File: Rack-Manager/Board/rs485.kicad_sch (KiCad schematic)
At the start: 0 parts

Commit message: Updated Texas Instruments and WIZnet KiCAD libraries. Continued with the schematics design.
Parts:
- added U8, U9: THVD1450DRBR, Texas Instruments:DRB0008F, symbol Texas Instruments:THVD1450DRBR

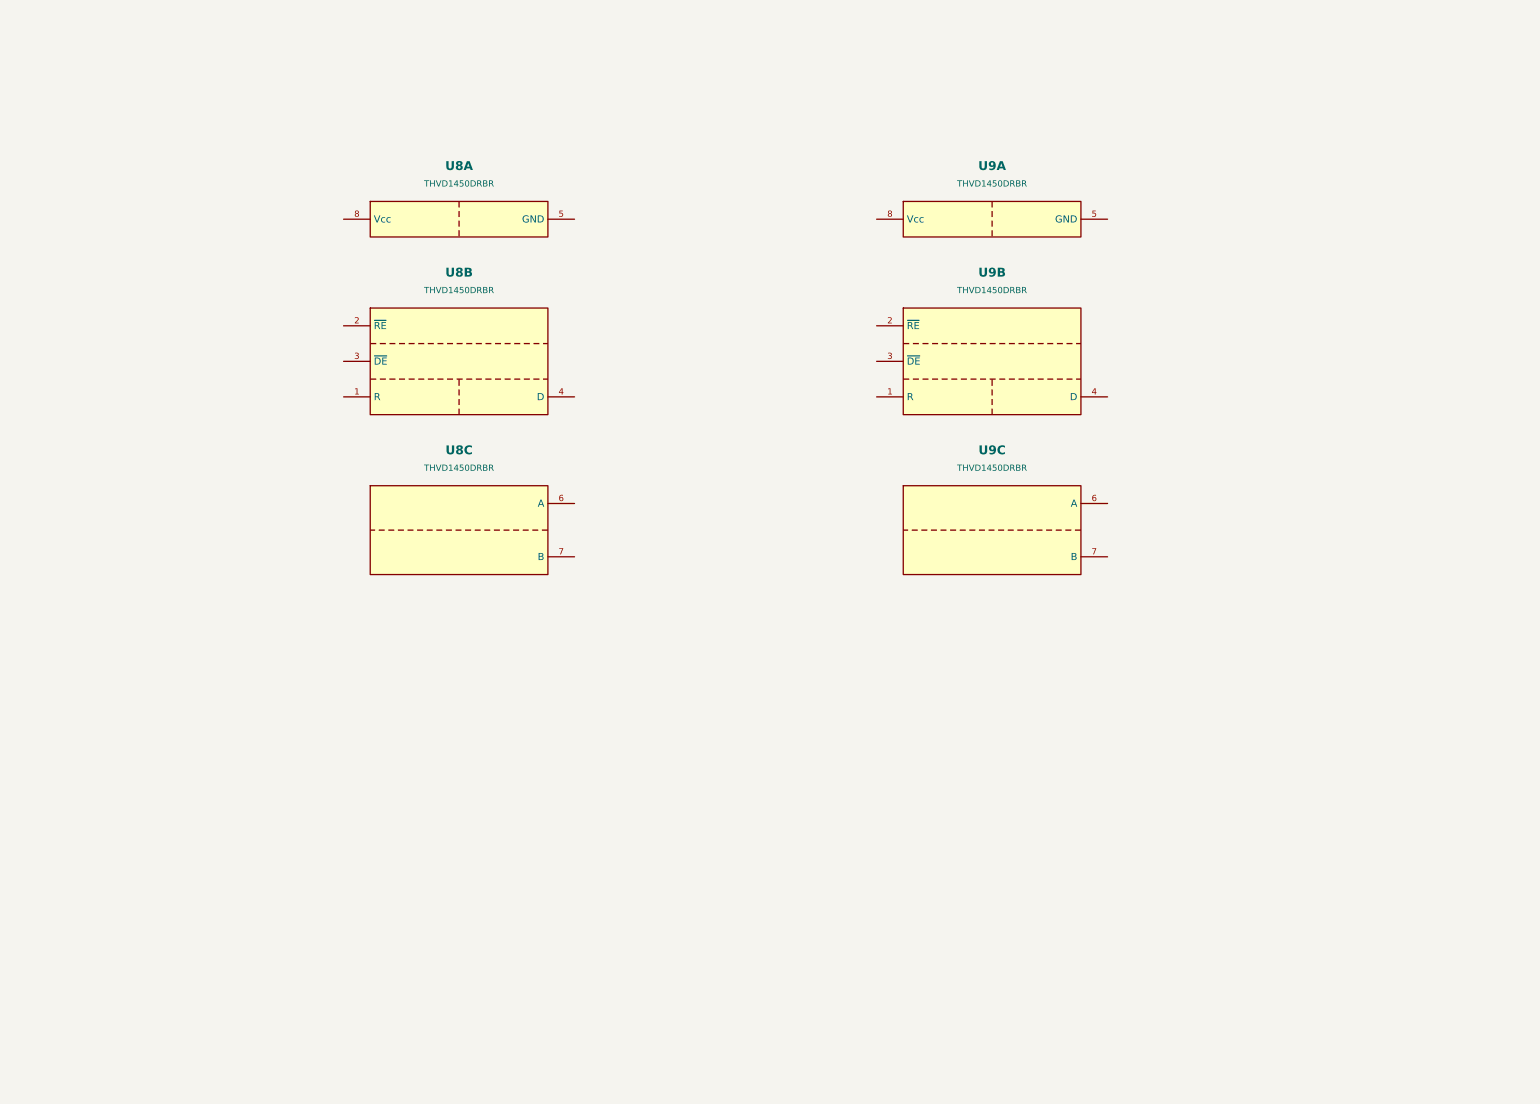
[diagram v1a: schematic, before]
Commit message: Updated Texas Instruments KiCAD library. Continued with the schematics design.
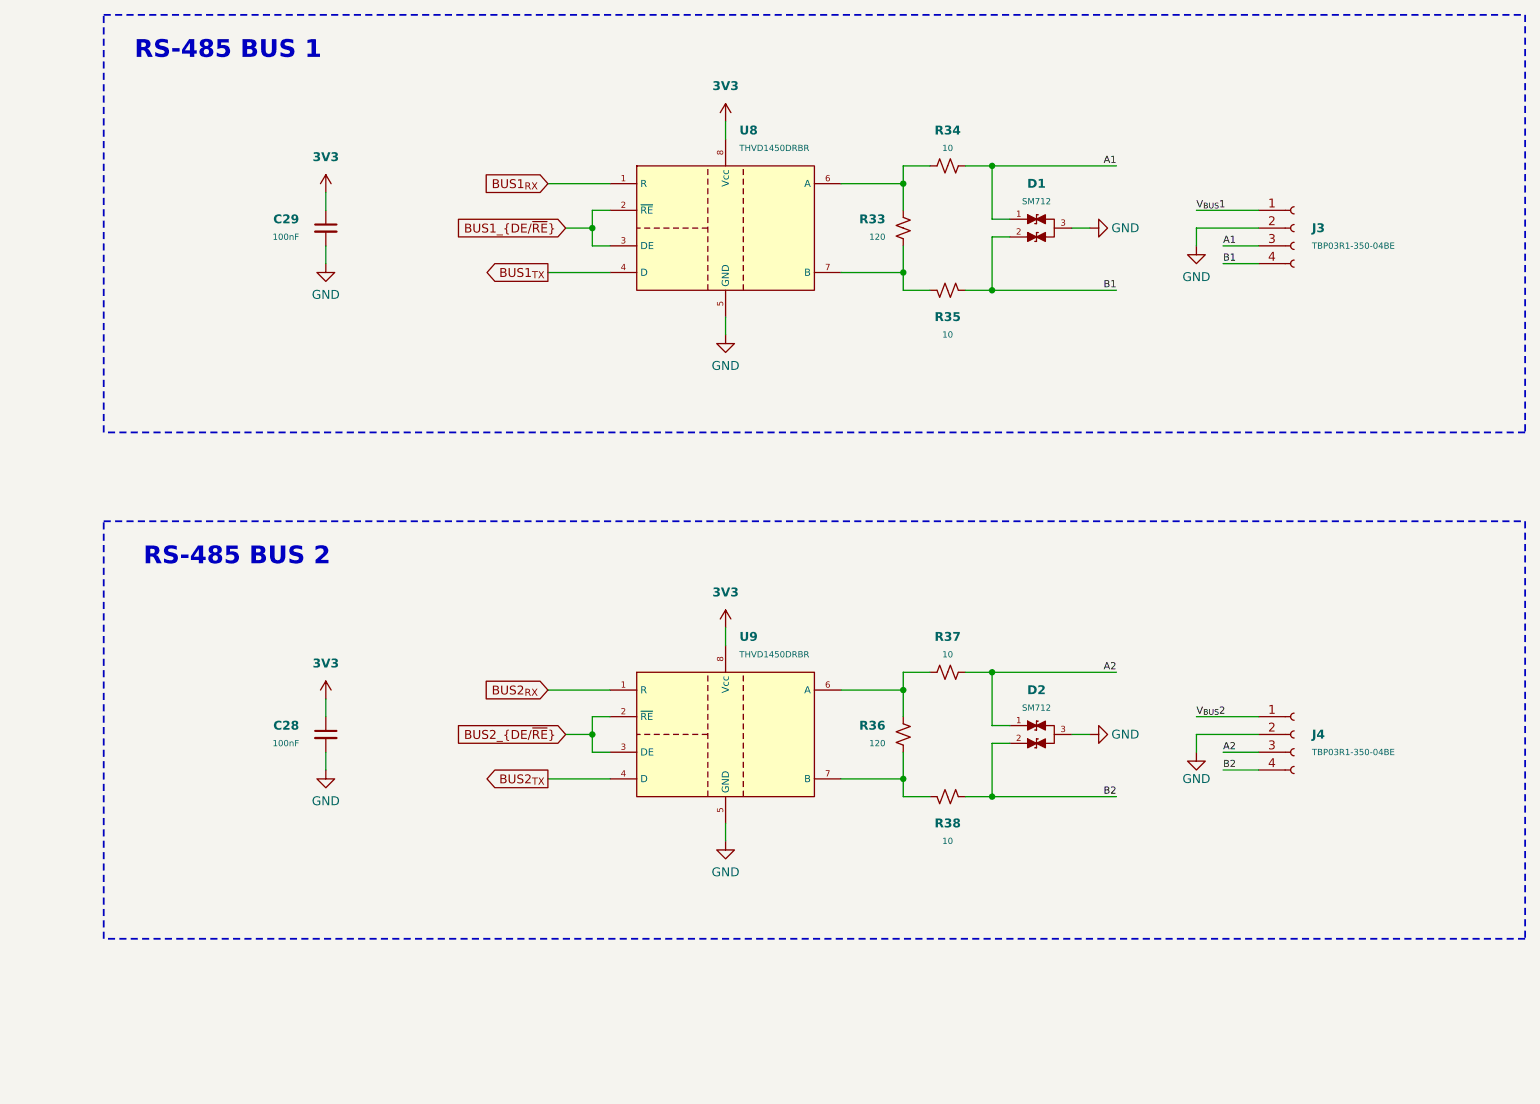
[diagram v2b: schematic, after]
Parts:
- removed unit 3 of U8
- removed unit 2 of U8
- removed unit 2 of U9
- removed unit 3 of U9
- added C28, C29: 100nF, Capacitor_SMD:C_0402_1005Metric, symbol Device:C_Small
- added D1, D2: SM712, Package_TO_SOT_SMD:SOT-23, symbol Diode:SM712_SOT23
- added J3, J4: TBP03R1-350-04BE, Same Sky:TBP03R1-350-04BE, symbol Connector:Conn_01x04_Socket
- added R33, R36: 120, Resistor_SMD:R_0603_1608Metric, symbol Device:R_Small_US
- added R34, R35, R37, R38: 10, Resistor_SMD:R_0402_1005Metric, symbol Device:R_Small_US
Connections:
- net GND: now reaches U9.5 (GND)
- net GND: now also U8.5 (GND), C28.2, C29.2, D1.3 (common), D2.3 (common), J3.2 (Pin_2), J4.2 (Pin_2)
- net 3V3: now reaches U9.8 (Vcc)
- net 3V3: now also U8.8 (Vcc), C28.1, C29.1
- new net: R36.2, R38.1, U9.7 (B)
- new net: R36.1, R37.1, U9.6 (A)
- new net: R33.1, R34.1, U8.6 (A)
- new net: R33.2, R35.1, U8.7 (B)
- new net A1: D1.1 (A1), J3.3 (Pin_3), R34.2
- new net A2: D2.1 (A1), J4.3 (Pin_3), R37.2
- new net B1: D1.2 (A2), J3.4 (Pin_4), R35.2
- new net B2: D2.2 (A2), J4.4 (Pin_4), R38.2
- new net BUS1_{DE/~{RE}}: U8.2 (~{RE}), U8.3 (DE)
- new net BUS1_{RX}: U8.1 (R)
- new net BUS1_{TX}: U8.4 (D)
- new net BUS2_{DE/~{RE}}: U9.2 (~{RE}), U9.3 (DE)
- new net BUS2_{RX}: U9.1 (R)
- new net BUS2_{TX}: U9.4 (D)
- new net V_{BUS}1: J3.1 (Pin_1)
- new net V_{BUS}2: J4.1 (Pin_1)
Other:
- note added: "RS-485 BUS 1"
- note added: "RS-485 BUS 2"
- title: (none) -> RS-485 Busses

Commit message: Continued with the schematic drawing.
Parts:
- renumbered C29 to C30, C28 to C31
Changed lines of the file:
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@@
 		(on_board yes)
 		(dnp no)
-		(property "Reference" "C28"
+		(property "Reference" "C31"
 			(at 78.74 125.73 0)
 			(effects
@@
 			(project "Rack-Manager"
 				(path "/5d42174d-da49-4bca-870b-353868af7168/9f35d409-1fd7-4241-ba93-dffedac70e6f"
-					(reference "C28")
+					(reference "C31")
 					(unit 1)
 				)
@@
 		(on_board yes)
 		(dnp no)
-		(property "Reference" "C29"
+		(property "Reference" "C30"
 			(at 78.74 53.34 0)
 			(effects
@@
 			(project "Rack-Manager"
 				(path "/5d42174d-da49-4bca-870b-353868af7168/9f35d409-1fd7-4241-ba93-dffedac70e6f"
-					(reference "C29")
-					(unit 1)
-				)
+					(reference "C30")
+					(unit 1)
+				)

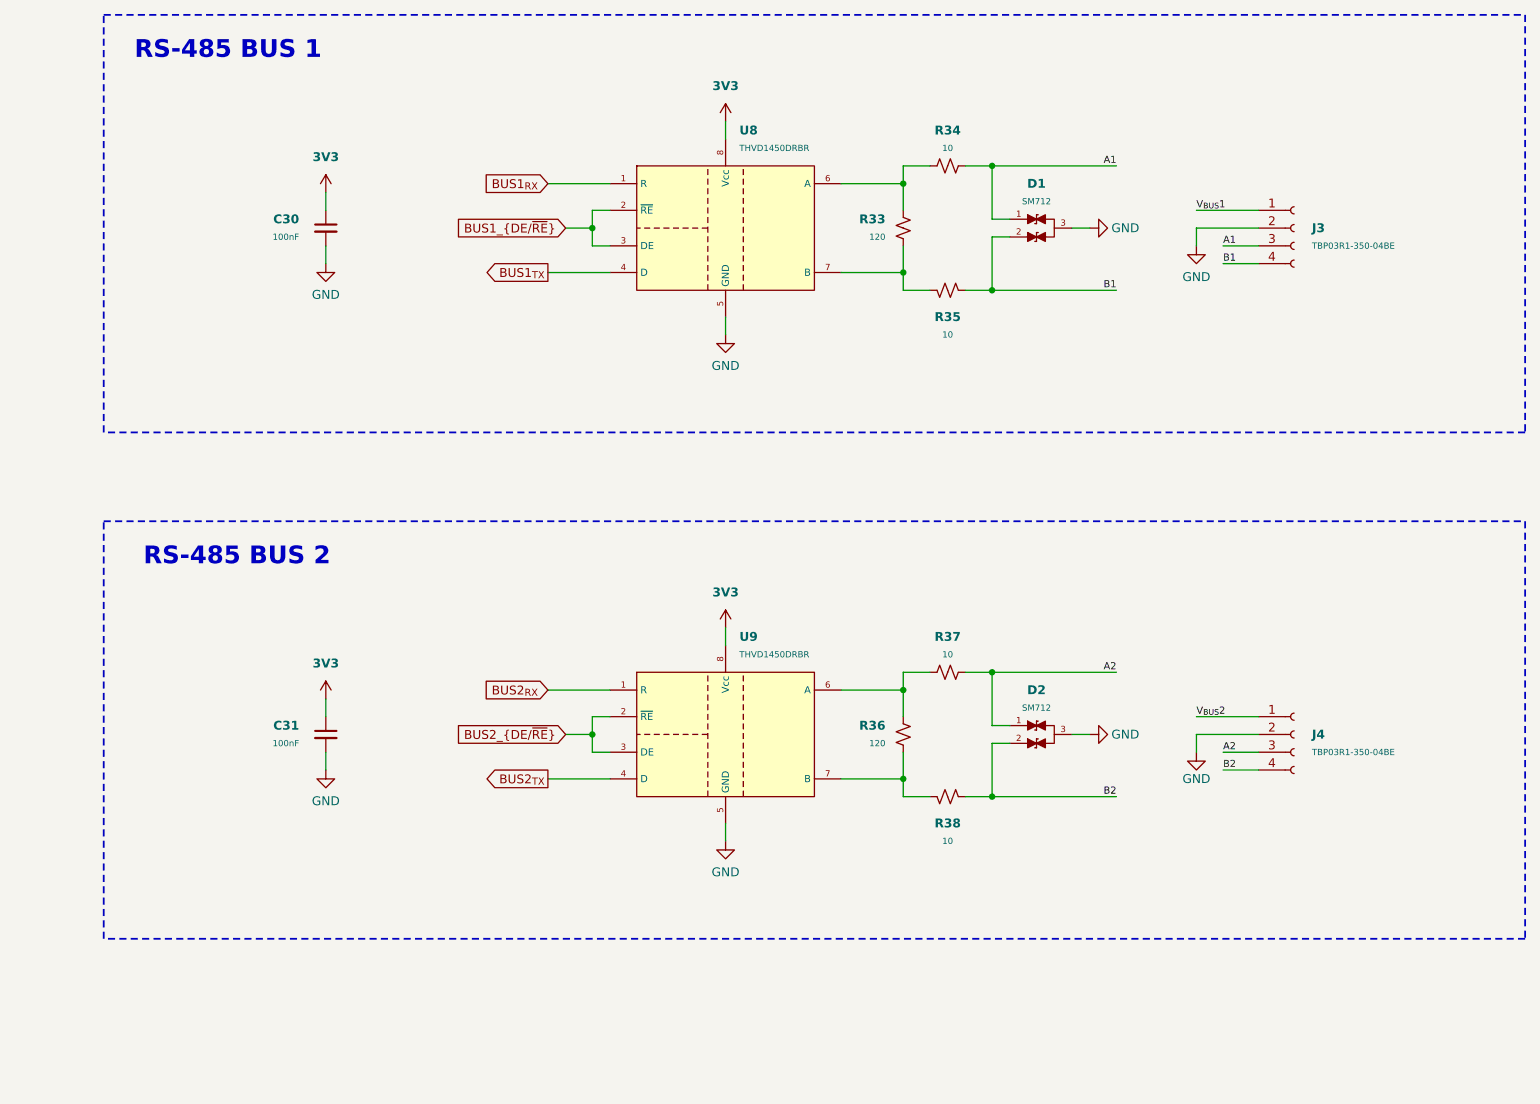
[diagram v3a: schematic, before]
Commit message: Added Bourns library, updated Texas Instruments library, continued with schematic drawing.
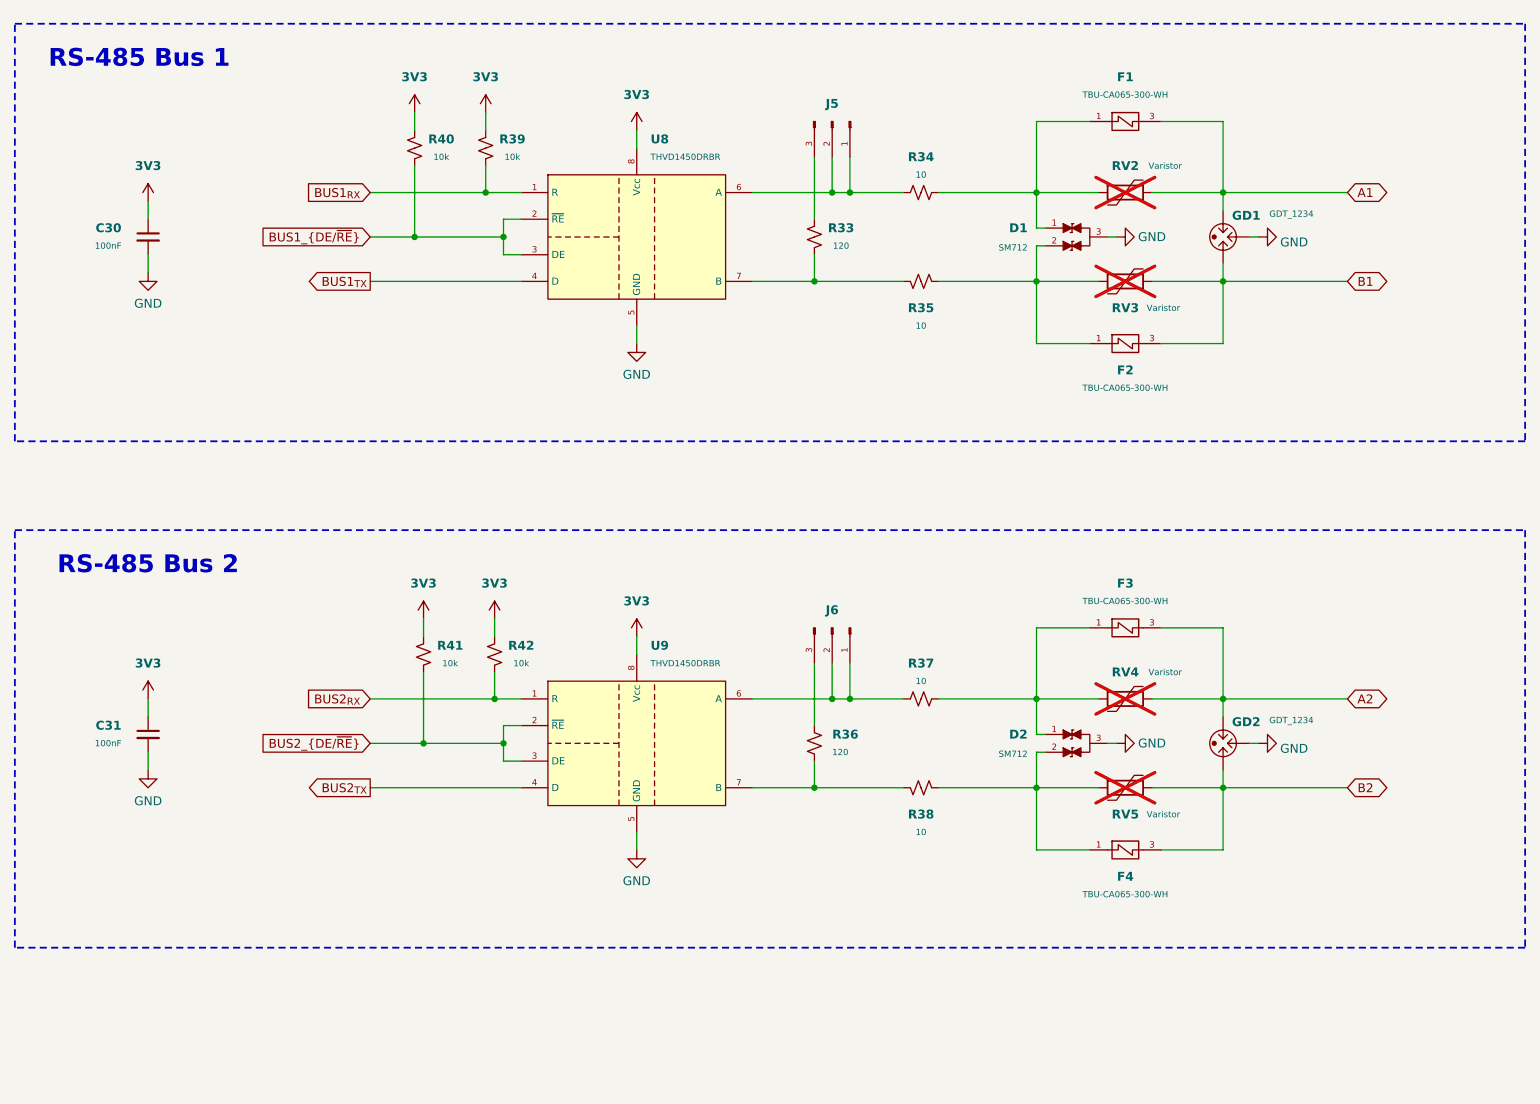
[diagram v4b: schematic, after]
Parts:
- removed J3, J4: TBP03R1-350-04BE, Same Sky:TBP03R1-350-04BE, symbol Connector:Conn_01x04_Socket
- added F1, F2, F3, F4: TBU-CA065-300-WH, Bourns:TBU-CA, symbol Bourns:TBU-CA
- added GD1, GD2: GDT_1234, symbol Device:GDT_3Pin
- added J5, J6: Conn_01x03_Pin, Connector_PinSocket_2.54mm:PinSocket_1x03_P2.54mm_Vertical, symbol Connector:Conn_01x03_Pin
- added R39, R40, R41, R42: 10k, Resistor_SMD:R_0402_1005Metric, symbol Device:R_Small_US
- added RV2, RV3, RV4, RV5: Varistor, symbol Device:Varistor
- R33: footprint Resistor_SMD:R_0603_1608Metric -> Resistor_SMD:R_0402_1005Metric
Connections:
- net 3V3: now also R39.2, R40.2, R41.2, R42.2
- net A1: now also F1.3, GD1.3, RV2.1; no longer D1.1 (A1), R34.2
- net A2: now also F3.3, GD2.3, RV4.1; no longer D2.1 (A1), R37.2
- net B1: now also F2.3, GD1.1, RV3.1; no longer D1.2 (A2), R35.2
- net B2: now also F4.3, GD2.1, RV5.1; no longer D2.2 (A2), R38.2
- net BUS1_{DE/~{RE}}: now also R40.1
- net BUS1_{RX}: now also R39.1
- net BUS2_{DE/~{RE}}: now also R41.1
- net BUS2_{RX}: now also R42.1
- net GND: now also GD1.2, GD2.2
- net at R37.1, U9.6 (A): now also J6.1 (Pin_1), J6.2 (Pin_2); no longer R36.1
- net at R34.1, U8.6 (A): now also J5.1 (Pin_1), J5.2 (Pin_2); no longer R33.1
- net at R35.1, U8.7 (B): now also R33.1; no longer R33.2
- new net: D2.2 (A2), F4.1, R38.2, RV5.2
- new net: D1.1 (A1), F1.1, R34.2, RV2.2
- new net: D2.1 (A1), F3.1, R37.2, RV4.2
- new net: J6.3 (Pin_3), R36.1
- new net: J5.3 (Pin_3), R33.2
- new net: D1.2 (A2), F2.1, R35.2, RV3.2
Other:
- note added: "RS-485 Bus 1"
- note added: "RS-485 Bus 2"
- note removed: "RS-485 BUS 1"
- note removed: "RS-485 BUS 2"
- title: RS-485 Busses -> RS-485 Transreceivers
- moved on the sheet: C30, C31, D1, R34, R35, R36, R37, R38, U8, U9
